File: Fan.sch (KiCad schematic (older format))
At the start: 9 parts, among them Q2 MOSFET_N, Q3 MOSFET_N, Q4 MOSFET_N, U6 MCP4922-E/P, U7 LM324

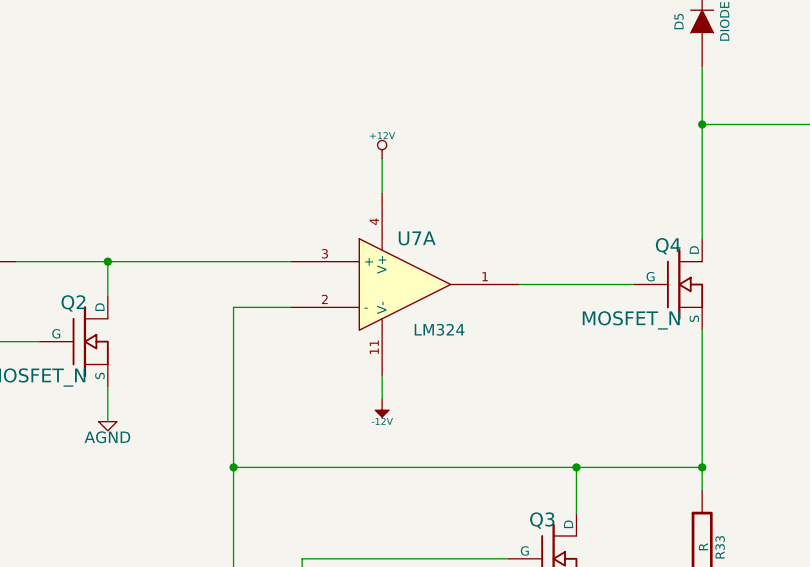
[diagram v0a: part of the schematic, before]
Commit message: THERMOCOUPLE 02-22-2014
Associated and placed PCB footprints of thermocouple modules in layout
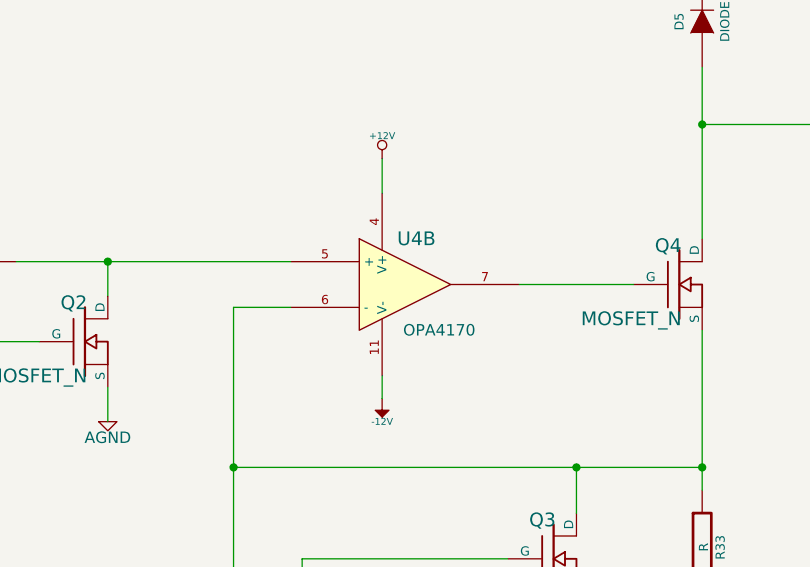
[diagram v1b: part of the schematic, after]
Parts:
- U4: renamed from U7; value LM324 -> OPA4170
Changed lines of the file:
@@
 Sheet 6 9
 Title ""
-Date "20 feb 2014"
+Date "23 feb 2014"
 Rev ""
 Comp ""
@@
 TACH
 $Comp
-L LM324 U7
-U 1 1 52F5F7EF
+L LM324 U4
+U 2 1 52F5F7EF
 P 6350 2750
-F 0 "U7" H 6400 2950 60  0000 C CNN
-F 1 "LM324" H 6500 2550 50  0000 C CNN
+F 0 "U4" H 6400 2950 60  0000 C CNN
+F 1 "OPA4170" H 6500 2550 50  0000 C CNN
 F 2 "~" H 6350 2750 60  0000 C CNN
 F 3 "~" H 6350 2750 60  0000 C CNN
-	1    6350 2750
+	2    6350 2750
 	1    0    0    -1
 $EndComp
@@
 $EndComp
 $Comp
-L AGND #PWR41
+L AGND #PWR044
 U 1 1 52F5F833
 P 7650 4400
-F 0 "#PWR41" H 7650 4400 40  0001 C CNN
+F 0 "#PWR044" H 7650 4400 40  0001 C CNN
 F 1 "AGND" H 7650 4330 50  0000 C CNN
 F 2 "" H 7650 4400 60  0000 C CNN
@@
 	5600 2850 5600 4300
 $Comp
-L -12V #PWR39
+L -12V #PWR045
 U 1 1 52F5F850
 P 6250 3250
-F 0 "#PWR39" H 6250 3380 20  0001 C CNN
+F 0 "#PWR045" H 6250 3380 20  0001 C CNN
 F 1 "-12V" H 6250 3350 30  0000 C CNN
 F 2 "" H 6250 3250 60  0000 C CNN
@@
 	6250 3150 6250 3250
 $Comp
-L +12V #PWR38
+L +12V #PWR046
 U 1 1 52F5F867
 P 6250 2200
-F 0 "#PWR38" H 6250 2150 20  0001 C CNN
+F 0 "#PWR046" H 6250 2150 20  0001 C CNN
 F 1 "+12V" H 6250 2300 30  0000 C CNN
 F 2 "" H 6250 2200 60  0000 C CNN
@@
 	6250 2200 6250 2350
 $Comp
-L AGND #PWR37
+L AGND #PWR047
 U 1 1 52F5F8F6
 P 5050 3350
-F 0 "#PWR37" H 5050 3350 40  0001 C CNN
+F 0 "#PWR047" H 5050 3350 40  0001 C CNN
 F 1 "AGND" H 5050 3280 50  0000 C CNN
 F 2 "" H 5050 3350 60  0000 C CNN
@@
 	5900 4750 2500 4750
 $Comp
-L +12C #PWR40
+L +12C #PWR048
 U 1 1 52F9D6B5
 P 7650 650
-F 0 "#PWR40" H 7650 620 30  0001 C CNN
+F 0 "#PWR048" H 7650 620 30  0001 C CNN
 F 1 "+12C" H 7650 760 40  0000 C CNN
 F 2 "" H 7650 650 60  0000 C CNN

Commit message: Fan Controller Module
1) Created and associated the footprints of fan controller module
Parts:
- removed Q3, Q4: MOSFET_N, ~, symbol MOSFET_N
- removed U6: MCP4922-E/P, DIP14, symbol MCP4922-E/P
- added C12, C13: C, ~, symbol C
- added Q3, Q4: NMOS, ~, symbol NMOS
- added U6: MCP4801, symbol MCP4801
- D5: value DIODE -> Schottky Diode; MFG NAME (none) -> Diodes Incorporated; MFG PART NUM (none) -> B130-13-F
- Q2: MFG NAME (none) -> Diodes Incorporated; MFG PART NUM (none) -> DMN65D8L-7
- TH5: value THERMISTOR -> PTC 0.5A; MFG NAME (none) -> TE Connectivity; MFG PART NUM (none) -> MINISMDC050F-2
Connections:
- net labels added: +5V, ~CS, ~LDAC, ~SHDN
- net labels removed: CS_N, MISO
- wire segments 31 -> 41
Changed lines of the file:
@@
 Sheet 6 9
 Title ""
-Date "23 feb 2014"
+Date "24 feb 2014"
 Rev ""
 Comp ""
@@
 	1    0    0    -1
 $EndComp
-$Comp
-L MOSFET_N Q4
-U 1 1 52F5F7FE
-P 7550 2750
-F 0 "Q4" H 7560 2920 60  0000 R CNN
-F 1 "MOSFET_N" H 7560 2600 60  0000 R CNN
-F 2 "~" H 7550 2750 60  0000 C CNN
-F 3 "~" H 7550 2750 60  0000 C CNN
-	1    7550 2750
-	1    0    0    -1
-$EndComp
 Wire Wire Line
 	6850 2750 7350 2750
@@
 Wire Wire Line
 	5050 3200 5050 3350
-$Comp
-L MCP4922-E/P U6
-U 1 1 52F5F90F
-P 3300 2800
-F 0 "U6" H 3450 3200 40  0000 L BNN
-F 1 "MCP4922-E/P" H 3450 3150 40  0000 L BNN
-F 2 "DIP14" H 3300 2800 30  0000 C CIN
-F 3 "" H 3300 2800 60  0000 C CNN
-	1    3300 2800
-	1    0    0    -1
-$EndComp
 Wire Wire Line
 	2500 5150 8650 5150
@@
 Wire Wire Line
 	4150 2650 3850 2650
-Text HLabel 2250 2600 0    60   Input ~ 0
+Text HLabel 1700 2650 0    60   Input ~ 0
 MOSI
-Text HLabel 2250 2900 0    60   Output ~ 0
-MISO
-Text HLabel 2250 2800 0    60   Input ~ 0
-CS_N
-Text HLabel 2250 2700 0    60   Input ~ 0
+Text HLabel 1700 2850 0    60   Input ~ 0
+~LDAC
+Text HLabel 1700 2250 0    60   Input ~ 0
+~CS
+Text HLabel 1700 2450 0    60   Input ~ 0
 SCLK
 Wire Wire Line
-	2250 2600 2750 2600
-Wire Wire Line
-	2750 2700 2250 2700
-Wire Wire Line
-	2250 2800 2750 2800
-$Comp
-L MOSFET_N Q3
-U 1 1 52F9D0E4
-P 7000 3950
-F 0 "Q3" H 7010 4120 60  0000 R CNN
-F 1 "MOSFET_N" H 7010 3800 60  0000 R CNN
-F 2 "~" H 7000 3950 60  0000 C CNN
-F 3 "~" H 7000 3950 60  0000 C CNN
-	1    7000 3950
-	1    0    0    -1
-$EndComp
+	1700 2650 2200 2650
+Wire Wire Line
+	2200 2450 1700 2450
+Wire Wire Line
+	1700 2250 2200 2250
 $Comp
 L THERMISTOR TH5
@@
 P 7650 950
 F 0 "TH5" V 7750 1000 50  0000 C CNN
-F 1 "THERMISTOR" V 7550 950 50  0000 C CNN
+F 1 "PTC 0.5A" V 7550 950 50  0000 C CNN
 F 2 "~" H 7650 950 60  0000 C CNN
 F 3 "~" H 7650 950 60  0000 C CNN
+F 4 "TE Connectivity" H 7650 950 60  0001 C CNN "MFG NAME"
+F 5 "MINISMDC050F-2" H 7650 950 60  0001 C CNN "MFG PART NUM"
 	1    7650 950
 	1    0    0    -1
@@
 P 7650 1600
 F 0 "D5" H 7650 1700 40  0000 C CNN
-F 1 "DIODE" H 7650 1500 40  0000 C CNN
+F 1 "Schottky Diode" H 7650 1500 40  0000 C CNN
 F 2 "~" H 7650 1600 60  0000 C CNN
 F 3 "~" H 7650 1600 60  0000 C CNN
+F 4 "Diodes Incorporated" H 7650 1600 60  0001 C CNN "MFG NAME"
+F 5 "B130-13-F" H 7650 1600 60  0001 C CNN "MFG PART NUM"
 	1    7650 1600
 	0    -1   -1   0
@@
 F 2 "~" H 4950 3000 60  0000 C CNN
 F 3 "~" H 4950 3000 60  0000 C CNN
+F 4 "Diodes Incorporated" H 4950 3000 60  0001 C CNN "MFG NAME"
+F 5 "DMN65D8L-7" H 4950 3000 60  0001 C CNN "MFG PART NUM"
 	1    4950 3000
 	1    0    0    -1
@@
 	1    0    0    -1
 $EndComp
+Text HLabel 1700 3000 0    60   Input ~ 0
+~SHDN
+Wire Wire Line
+	1700 2850 2200 2850
+Wire Wire Line
+	1700 3000 2200 3000
+$Comp
+L +5V #PWR049
+U 1 1 530B6076
+P 3000 1700
+F 0 "#PWR049" H 3000 1790 20  0001 C CNN
+F 1 "+5V" H 3000 1790 30  0000 C CNN
+F 2 "" H 3000 1700 60  0000 C CNN
+F 3 "" H 3000 1700 60  0000 C CNN
+	1    3000 1700
+	-1   0    0    -1
+$EndComp
+Wire Wire Line
+	3000 1700 3000 1850
+$Comp
+L C C12
+U 1 1 530B607D
+P 2700 1750
+F 0 "C12" H 2700 1850 40  0000 L CNN
+F 1 "C" H 2706 1665 40  0000 L CNN
+F 2 "~" H 2738 1600 30  0000 C CNN
+F 3 "~" H 2700 1750 60  0000 C CNN
+	1    2700 1750
+	0    1    -1   0
+$EndComp
+Wire Wire Line
+	2900 1750 3000 1750
+Connection ~ 3000 1750
+$Comp
+L AGND #PWR050
+U 1 1 530B6085
+P 2400 1850
+F 0 "#PWR050" H 2400 1850 40  0001 C CNN
+F 1 "AGND" H 2400 1780 50  0000 C CNN
+F 2 "" H 2400 1850 60  0000 C CNN
+F 3 "" H 2400 1850 60  0000 C CNN
+	1    2400 1850
+	-1   0    0    -1
+$EndComp
+Wire Wire Line
+	2400 1750 2500 1750
+Wire Wire Line
+	2400 1750 2400 1850
+$Comp
+L MCP4801 U6
+U 1 1 530B60FB
+P 3000 2900
+F 0 "U6" H 2550 3700 60  0000 C CNN
+F 1 "MCP4801" H 3000 3150 60  0000 C CNN
+F 2 "" H 4700 2100 60  0000 C CNN
+F 3 "" H 4700 2100 60  0000 C CNN
+	1    3000 2900
+	1    0    0    -1
+$EndComp
+$Comp
+L AGND #PWR051
+U 1 1 530B6108
+P 3000 3600
+F 0 "#PWR051" H 3000 3600 40  0001 C CNN
+F 1 "AGND" H 3000 3530 50  0000 C CNN
+F 2 "" H 3000 3600 60  0000 C CNN
+F 3 "" H 3000 3600 60  0000 C CNN
+	1    3000 3600
+	1    0    0    -1
+$EndComp
+Wire Wire Line
+	3000 3450 3000 3600
+$Comp
+L C C13
+U 1 1 530B64EA
+P 8050 700
+F 0 "C13" H 8050 800 40  0000 L CNN
+F 1 "C" H 8056 615 40  0000 L CNN
+F 2 "~" H 8088 550 30  0000 C CNN
+F 3 "~" H 8050 700 60  0000 C CNN
+	1    8050 700
+	0    -1   -1   0
+$EndComp
+Wire Wire Line
+	7850 700  7650 700
+Wire Wire Line
+	8250 700  8350 700
+Wire Wire Line
+	8350 700  8350 800
+$Comp
+L AGND #PWR052
+U 1 1 530B655B
+P 8350 800
+F 0 "#PWR052" H 8350 800 40  0001 C CNN
+F 1 "AGND" H 8350 730 50  0000 C CNN
+F 2 "" H 8350 800 60  0000 C CNN
+F 3 "" H 8350 800 60  0000 C CNN
+	1    8350 800
+	1    0    0    -1
+$EndComp
+$Comp
+L NMOS Q4
+U 1 1 530B70BC
+P 7550 2750
+F 0 "Q4" H 7560 2920 60  0000 R CNN
+F 1 "NMOS" H 7560 2600 60  0000 R CNN
+F 2 "~" H 7550 2750 60  0000 C CNN
+F 3 "~" H 7550 2750 60  0000 C CNN
+F 4 "Alpha & Omega Semiconductor Inc" H 7550 2750 60  0001 C CNN "MFG NAME"
+F 5 "AOD476" H 7550 2750 60  0001 C CNN "MFG PART NUM"
+	1    7550 2750
+	1    0    0    -1
+$EndComp
+$Comp
+L NMOS Q3
+U 1 1 530B70CB
+P 7000 3950
+F 0 "Q3" H 7010 4120 60  0000 R CNN
+F 1 "NMOS" H 7010 3800 60  0000 R CNN
+F 2 "~" H 7000 3950 60  0000 C CNN
+F 3 "~" H 7000 3950 60  0000 C CNN
+F 4 "Alpha & Omega Semiconductor Inc" H 7000 3950 60  0001 C CNN "MFG NAME"
+F 5 "AOD476" H 7000 3950 60  0001 C CNN "MFG PART NUM"
+	1    7000 3950
+	1    0    0    -1
+$EndComp

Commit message: Layout v1.0
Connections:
- net AGND: no longer C13.2, Q3.3, R33.2
- net +12V renamed FE_V+
- net -12V renamed FE_V-
- new net GND: C13.2, Q3.3, R33.2
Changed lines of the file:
@@
 Sheet 6 9
 Title ""
-Date "28 feb 2014"
+Date "3 mar 2014"
 Rev ""
 Comp ""
@@
 	1    0    0    -1
 $EndComp
-$Comp
-L AGND #PWR044
-U 1 1 52F5F833
-P 7650 4400
-F 0 "#PWR044" H 7650 4400 40  0001 C CNN
-F 1 "AGND" H 7650 4330 50  0000 C CNN
-F 2 "" H 7650 4400 60  0000 C CNN
-F 3 "" H 7650 4400 60  0000 C CNN
-	1    7650 4400
-	1    0    0    -1
-$EndComp
 Wire Wire Line
 	7650 4150 7650 4400
@@
 Wire Wire Line
 	5600 2850 5600 4300
-$Comp
-L -12V #PWR045
-U 1 1 52F5F850
-P 6250 3250
-F 0 "#PWR045" H 6250 3380 20  0001 C CNN
-F 1 "-12V" H 6250 3350 30  0000 C CNN
-F 2 "" H 6250 3250 60  0000 C CNN
-F 3 "" H 6250 3250 60  0000 C CNN
-	1    6250 3250
-	-1   0    0    1
-$EndComp
 Wire Wire Line
 	6250 3150 6250 3250
-$Comp
-L +12V #PWR046
-U 1 1 52F5F867
-P 6250 2200
-F 0 "#PWR046" H 6250 2150 20  0001 C CNN
-F 1 "+12V" H 6250 2300 30  0000 C CNN
-F 2 "" H 6250 2200 60  0000 C CNN
-F 3 "" H 6250 2200 60  0000 C CNN
-	1    6250 2200
-	1    0    0    -1
-$EndComp
 Wire Wire Line
 	6250 2200 6250 2350
 $Comp
-L AGND #PWR047
+L AGND #PWR041
 U 1 1 52F5F8F6
 P 5050 3350
-F 0 "#PWR047" H 5050 3350 40  0001 C CNN
+F 0 "#PWR041" H 5050 3350 40  0001 C CNN
 F 1 "AGND" H 5050 3280 50  0000 C CNN
 F 2 "" H 5050 3350 60  0000 C CNN
@@
 	5900 4750 2500 4750
 $Comp
-L +12C #PWR048
+L +12C #PWR042
 U 1 1 52F9D6B5
 P 7650 650
-F 0 "#PWR048" H 7650 620 30  0001 C CNN
+F 0 "#PWR042" H 7650 620 30  0001 C CNN
 F 1 "+12C" H 7650 760 40  0000 C CNN
 F 2 "" H 7650 650 60  0000 C CNN
@@
 	1700 3000 2200 3000
 $Comp
-L +5V #PWR049
+L +5V #PWR043
 U 1 1 530B6076
 P 3000 1700
-F 0 "#PWR049" H 3000 1790 20  0001 C CNN
+F 0 "#PWR043" H 3000 1790 20  0001 C CNN
 F 1 "+5V" H 3000 1790 30  0000 C CNN
 F 2 "" H 3000 1700 60  0000 C CNN
@@
 Connection ~ 3000 1750
 $Comp
-L AGND #PWR050
+L AGND #PWR044
 U 1 1 530B6085
 P 2400 1850
-F 0 "#PWR050" H 2400 1850 40  0001 C CNN
+F 0 "#PWR044" H 2400 1850 40  0001 C CNN
 F 1 "AGND" H 2400 1780 50  0000 C CNN
 F 2 "" H 2400 1850 60  0000 C CNN
@@
 $EndComp
 $Comp
-L AGND #PWR051
+L AGND #PWR045
 U 1 1 530B6108
 P 3000 3600
-F 0 "#PWR051" H 3000 3600 40  0001 C CNN
+F 0 "#PWR045" H 3000 3600 40  0001 C CNN
 F 1 "AGND" H 3000 3530 50  0000 C CNN
 F 2 "" H 3000 3600 60  0000 C CNN
@@
 Wire Wire Line
 	8350 700  8350 800
-$Comp
-L AGND #PWR052
-U 1 1 530B655B
-P 8350 800
-F 0 "#PWR052" H 8350 800 40  0001 C CNN
-F 1 "AGND" H 8350 730 50  0000 C CNN
-F 2 "" H 8350 800 60  0000 C CNN
-F 3 "" H 8350 800 60  0000 C CNN
-	1    8350 800
-	1    0    0    -1
-$EndComp
 $Comp
 L NMOS Q4
@@
 	1    0    0    -1
 $EndComp
+$Comp
+L FE_V- #PWR51
+U 1 1 5312A372
+P 6250 3250
+F 0 "#PWR51" H 6250 3450 40  0001 C CNN
+F 1 "FE_V-" H 6250 3400 40  0000 C CNN
+F 2 "" H 6250 3250 60  0000 C CNN
+F 3 "" H 6250 3250 60  0000 C CNN
+	1    6250 3250
+	-1   0    0    1
+$EndComp
+$Comp
+L FE_V+ #PWR046
+U 1 1 5312A378
+P 6250 2200
+F 0 "#PWR046" H 6250 2300 30  0001 C CNN
+F 1 "FE_V+" H 6250 2300 30  0000 C CNN
+F 2 "" H 6250 2200 60  0000 C CNN
+F 3 "" H 6250 2200 60  0000 C CNN
+	1    6250 2200
+	1    0    0    -1
+$EndComp
+$Comp
+L GND #PWR047
+U 1 1 5312E9EE
+P 7650 4400
+F 0 "#PWR047" H 7650 4400 30  0001 C CNN
+F 1 "GND" H 7650 4330 30  0001 C CNN
+F 2 "" H 7650 4400 60  0000 C CNN
+F 3 "" H 7650 4400 60  0000 C CNN
+	1    7650 4400
+	1    0    0    -1
+$EndComp
+$Comp
+L GND #PWR048
+U 1 1 5312E9FD
+P 8350 800
+F 0 "#PWR048" H 8350 800 30  0001 C CNN
+F 1 "GND" H 8350 730 30  0001 C CNN
+F 2 "" H 8350 800 60  0000 C CNN
+F 3 "" H 8350 800 60  0000 C CNN
+	1    8350 800
+	1    0    0    -1
+$EndComp

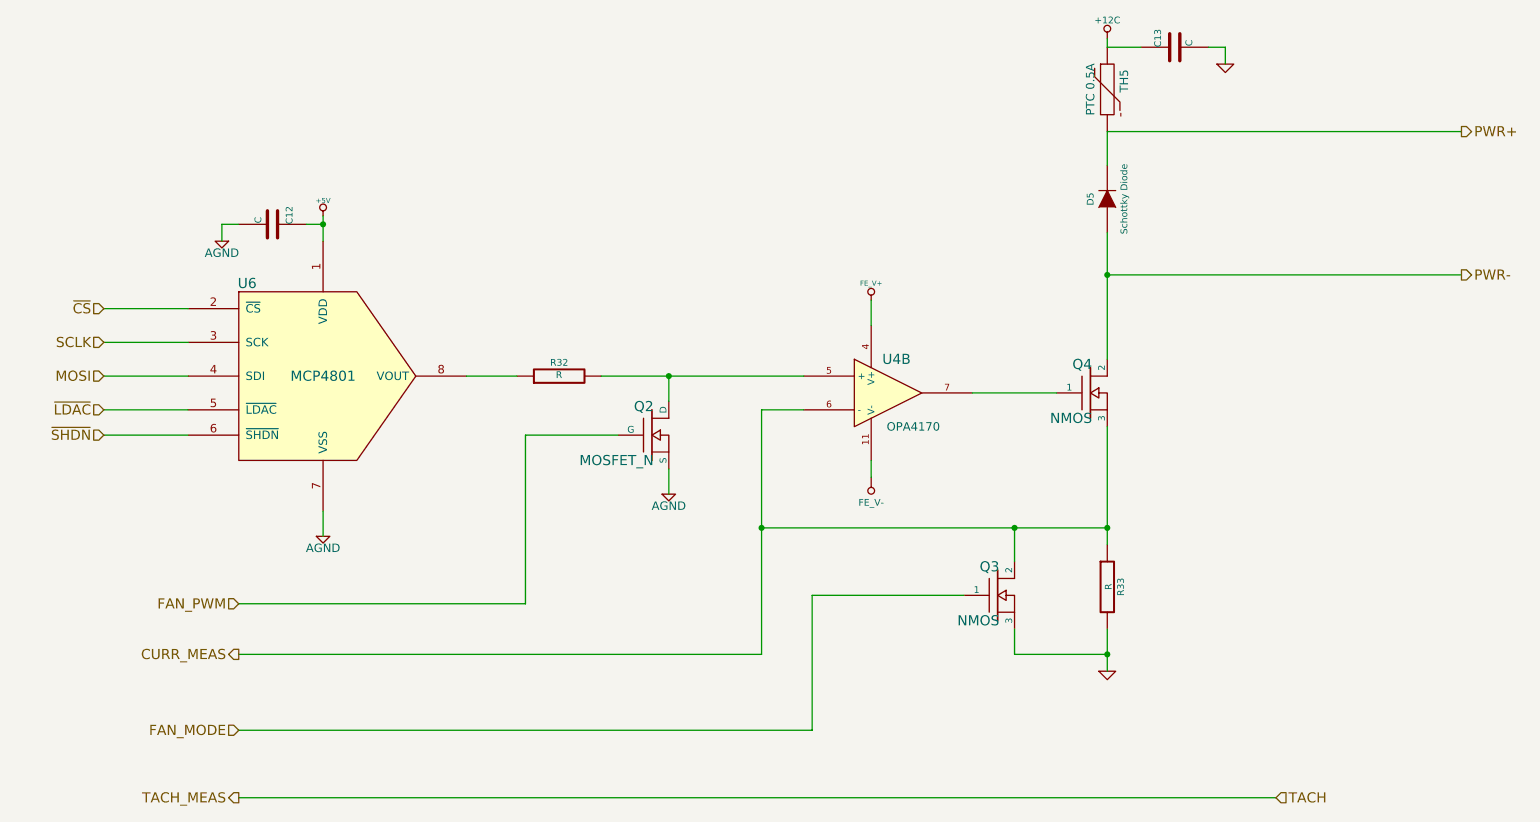
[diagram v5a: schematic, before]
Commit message: Layout v4.0
Adding ground planes according to location of modules
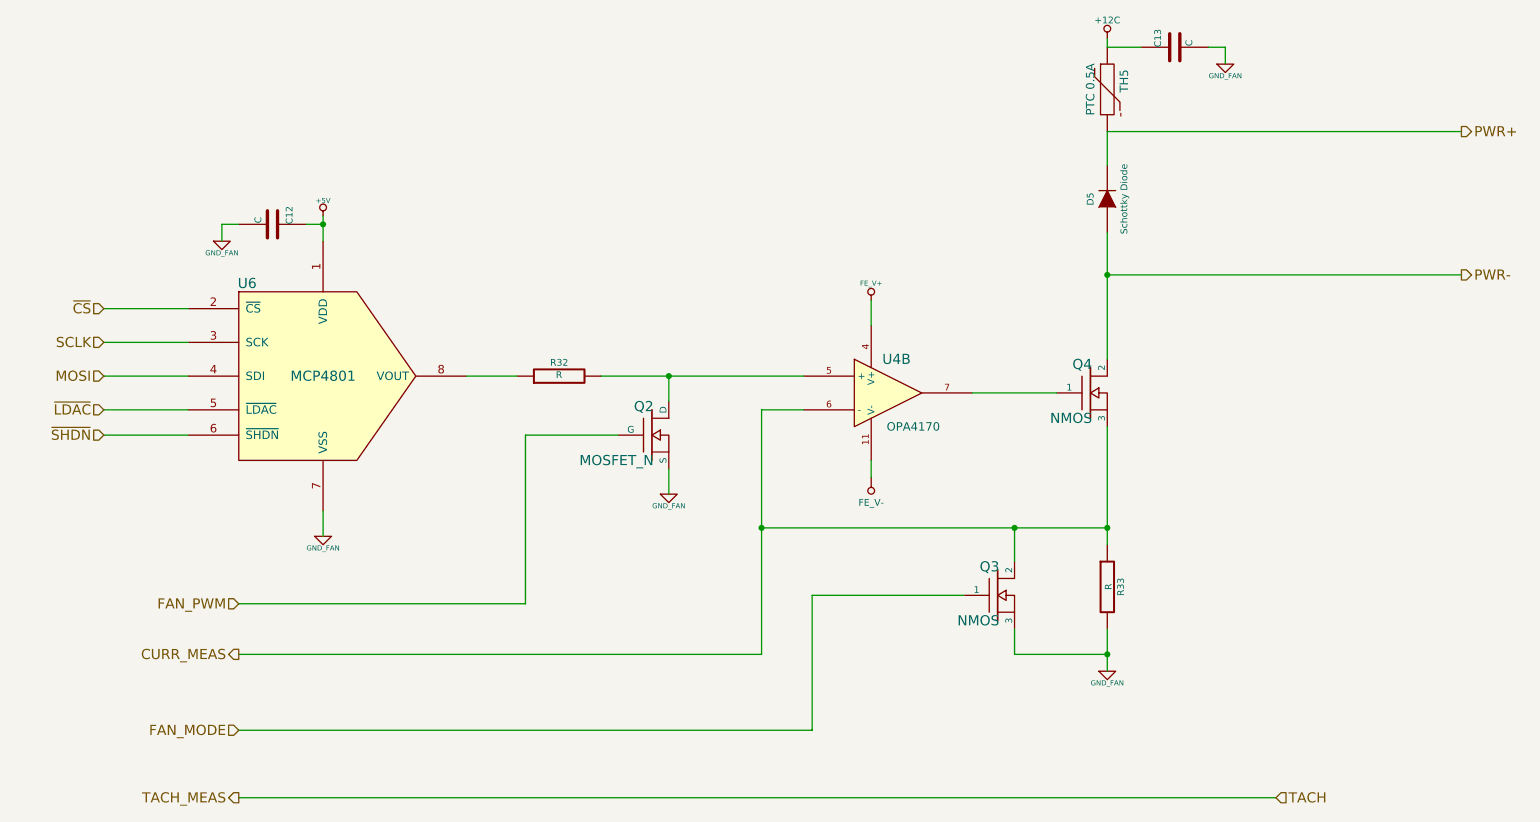
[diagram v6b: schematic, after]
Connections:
- net GND is gone; now on net GND_FAN: C13.2, Q3.3, R33.2
- net AGND renamed GND_FAN
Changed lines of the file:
@@
 Sheet 6 9
 Title ""
-Date "3 mar 2014"
+Date "6 mar 2014"
 Rev ""
 Comp ""
@@
 Wire Wire Line
 	6250 2200 6250 2350
-$Comp
-L AGND #PWR041
-U 1 1 52F5F8F6
-P 5050 3350
-F 0 "#PWR041" H 5050 3350 40  0001 C CNN
-F 1 "AGND" H 5050 3280 50  0000 C CNN
-F 2 "" H 5050 3350 60  0000 C CNN
-F 3 "" H 5050 3350 60  0000 C CNN
-	1    5050 3350
-	1    0    0    -1
-$EndComp
 Wire Wire Line
 	5050 3200 5050 3350
@@
 	5900 4750 2500 4750
 $Comp
-L +12C #PWR042
+L +12C #PWR041
 U 1 1 52F9D6B5
 P 7650 650
-F 0 "#PWR042" H 7650 620 30  0001 C CNN
+F 0 "#PWR041" H 7650 620 30  0001 C CNN
 F 1 "+12C" H 7650 760 40  0000 C CNN
 F 2 "" H 7650 650 60  0000 C CNN
@@
 	1700 3000 2200 3000
 $Comp
-L +5V #PWR043
+L +5V #PWR042
 U 1 1 530B6076
 P 3000 1700
-F 0 "#PWR043" H 3000 1790 20  0001 C CNN
+F 0 "#PWR042" H 3000 1790 20  0001 C CNN
 F 1 "+5V" H 3000 1790 30  0000 C CNN
 F 2 "" H 3000 1700 60  0000 C CNN
@@
 	2900 1750 3000 1750
 Connection ~ 3000 1750
-$Comp
-L AGND #PWR044
-U 1 1 530B6085
-P 2400 1850
-F 0 "#PWR044" H 2400 1850 40  0001 C CNN
-F 1 "AGND" H 2400 1780 50  0000 C CNN
-F 2 "" H 2400 1850 60  0000 C CNN
-F 3 "" H 2400 1850 60  0000 C CNN
-	1    2400 1850
-	-1   0    0    -1
-$EndComp
 Wire Wire Line
 	2400 1750 2500 1750
@@
 F 3 "" H 4700 2100 60  0000 C CNN
 	1    3000 2900
-	1    0    0    -1
-$EndComp
-$Comp
-L AGND #PWR045
-U 1 1 530B6108
-P 3000 3600
-F 0 "#PWR045" H 3000 3600 40  0001 C CNN
-F 1 "AGND" H 3000 3530 50  0000 C CNN
-F 2 "" H 3000 3600 60  0000 C CNN
-F 3 "" H 3000 3600 60  0000 C CNN
-	1    3000 3600
 	1    0    0    -1
 $EndComp
@@
 $EndComp
 $Comp
-L FE_V+ #PWR046
+L FE_V+ #PWR043
 U 1 1 5312A378
 P 6250 2200
-F 0 "#PWR046" H 6250 2300 30  0001 C CNN
+F 0 "#PWR043" H 6250 2300 30  0001 C CNN
 F 1 "FE_V+" H 6250 2300 30  0000 C CNN
 F 2 "" H 6250 2200 60  0000 C CNN
@@
 $EndComp
 $Comp
-L GND #PWR047
-U 1 1 5312E9EE
+L GND_FAN #PWR044
+U 1 1 53183257
 P 7650 4400
-F 0 "#PWR047" H 7650 4400 30  0001 C CNN
-F 1 "GND" H 7650 4330 30  0001 C CNN
+F 0 "#PWR044" H 7650 4400 30  0001 C CNN
+F 1 "GND_FAN" H 7650 4330 30  0000 C CNN
 F 2 "" H 7650 4400 60  0000 C CNN
 F 3 "" H 7650 4400 60  0000 C CNN
@@
 $EndComp
 $Comp
-L GND #PWR048
-U 1 1 5312E9FD
+L GND_FAN #PWR045
+U 1 1 53183270
 P 8350 800
-F 0 "#PWR048" H 8350 800 30  0001 C CNN
-F 1 "GND" H 8350 730 30  0001 C CNN
+F 0 "#PWR045" H 8350 800 30  0001 C CNN
+F 1 "GND_FAN" H 8350 730 30  0000 C CNN
 F 2 "" H 8350 800 60  0000 C CNN
 F 3 "" H 8350 800 60  0000 C CNN
@@
 	1    0    0    -1
 $EndComp
+$Comp
+L GND_FAN #PWR046
+U 1 1 5318327F
+P 5050 3350
+F 0 "#PWR046" H 5050 3350 30  0001 C CNN
+F 1 "GND_FAN" H 5050 3280 30  0000 C CNN
+F 2 "" H 5050 3350 60  0000 C CNN
+F 3 "" H 5050 3350 60  0000 C CNN
+	1    5050 3350
+	1    0    0    -1
+$EndComp
+$Comp
+L GND_FAN #PWR047
+U 1 1 5318328E
+P 3000 3600
+F 0 "#PWR047" H 3000 3600 30  0001 C CNN
+F 1 "GND_FAN" H 3000 3530 30  0000 C CNN
+F 2 "" H 3000 3600 60  0000 C CNN
+F 3 "" H 3000 3600 60  0000 C CNN
+	1    3000 3600
+	1    0    0    -1
+$EndComp
+$Comp
+L GND_FAN #PWR048
+U 1 1 5318329D
+P 2400 1850
+F 0 "#PWR048" H 2400 1850 30  0001 C CNN
+F 1 "GND_FAN" H 2400 1780 30  0000 C CNN
+F 2 "" H 2400 1850 60  0000 C CNN
+F 3 "" H 2400 1850 60  0000 C CNN
+	1    2400 1850
+	1    0    0    -1
+$EndComp
